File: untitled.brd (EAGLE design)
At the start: 42.2 x 27.9 mm, 15 parts, among them IC1 ACS758LCB-050B-PFF-T, IC2 LM2936DT-3.3

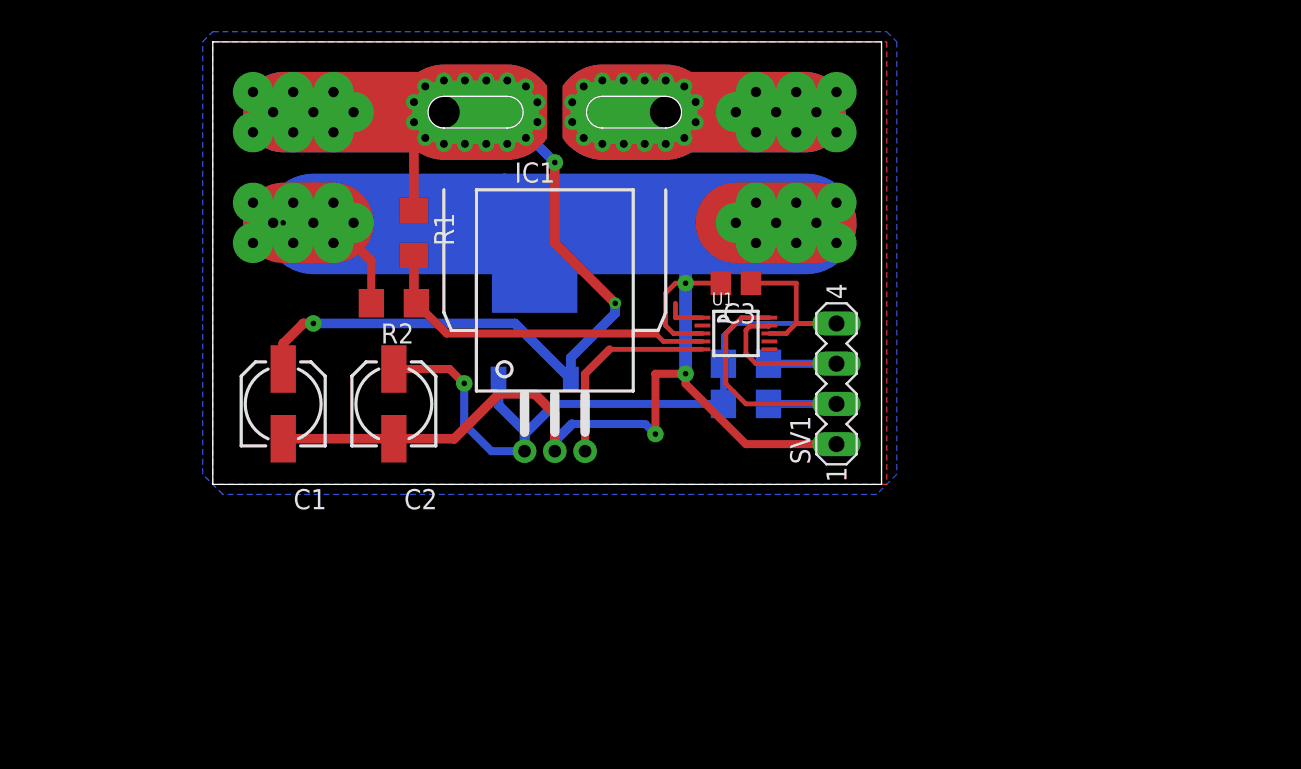
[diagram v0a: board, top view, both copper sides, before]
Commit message: Add new schematic for new dc dc converter
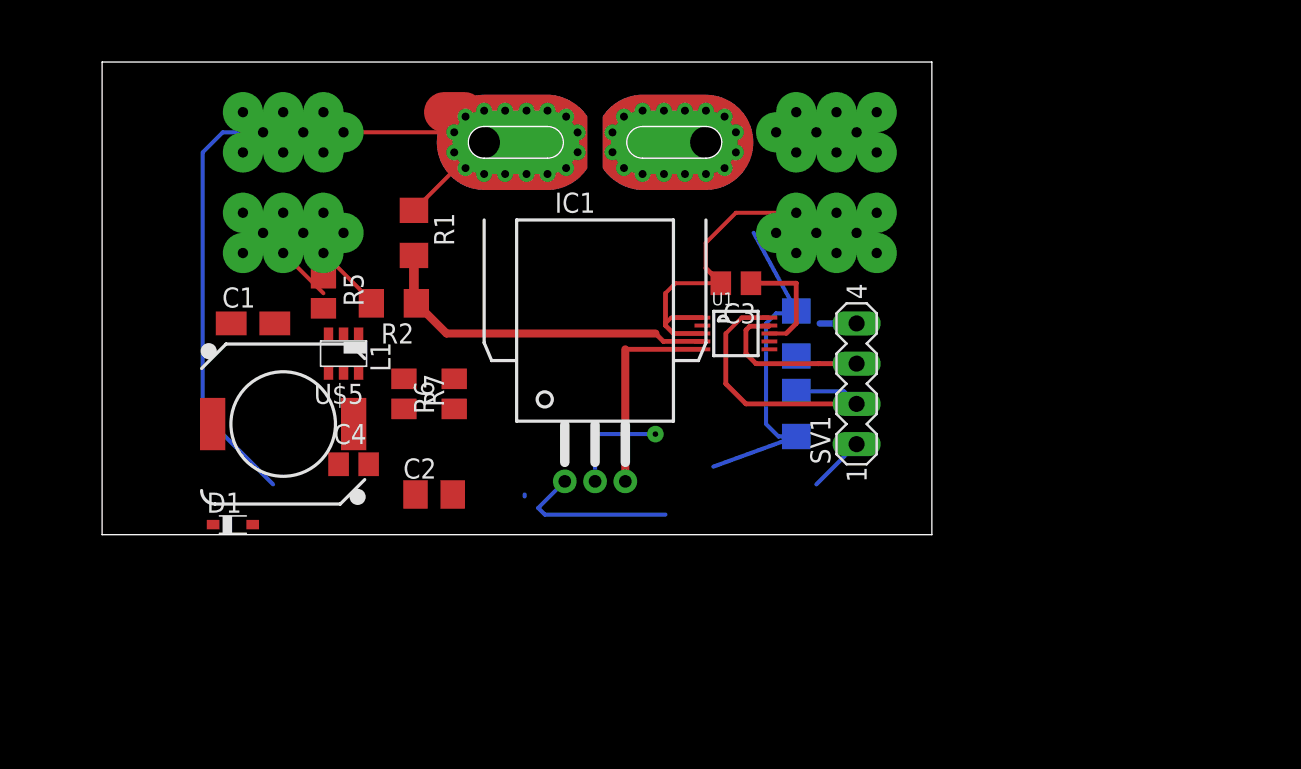
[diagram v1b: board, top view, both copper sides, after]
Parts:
- removed IC2: LM2936DT-3.3, national-semiconductor:TO252
- added C4: 100nF, rcl:C0805
- added D1: MBRS1100T3G, diode:SOD323_ST
- added L1: SRU1048-470Y, inductors:DR1030
- added R5: 100k, rcl:M0805
- added R6: 33k1, rcl:M0805
- added R7: 10k, rcl:M0805
- added U$5: LMR16006, texas:TSOT23-6_DDC
- C1: value (none) -> 2.2uF 12061C225K4T2A; device rcl:153CLV-0505 -> rcl:A/3216-18R
- C2: value (none) -> 22uF C2012X5R1C226M125AC; device rcl:153CLV-0505 -> rcl:R/2012-12R
- moved C2 6.25 mm to (15.2, 21.6), turned to 0 degrees
- moved C1 5.43 mm to (3.81, 32.4), turned to 0 degrees
- moved R4 3.70 mm to (38.1, 31.8), turned to 90 degrees
- moved R3 3.24 mm to (38.1, 26.7), turned to 270 degrees
- moved IC1 3.18 mm to (25.4, 43.8)
- moved U$1 2.84 mm to (34.3, 44.5)
- moved U$4 2.62 mm to (34.3, 38.1)
- moved U$3 1.42 mm to (12.1, 44.5)
- moved SV1 1.27 mm to (41.9, 28.6)
- moved U$2 0.90 mm to (12.1, 38.1)
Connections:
- new net N$10: C4.2, U$5.1
- new net N$11: R6.2, R7.1, U$5.3
- new net N$3: R5.1, U$5.4
- new net N$9: C4.1, D1.C, L1.2, U$5.6
- net GND: now also D1.A, R7.2, U$5.2; no longer IC2.2
- net N$4: now also R5.2, U$5.5; no longer IC2.1
- net VCC: now also L1.1, R6.1; no longer IC2.3
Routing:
- net GND: track 140.7 -> 44.0 mm, vias 4 -> 2
- net N$4: track 78.7 -> 45.3 mm, vias 3 -> 0
- net N$2: track 17.7 -> 0.08 mm
- net VCC: track 53.2 -> 42.4 mm, vias 1 -> 0
- net N$6: track 18.1 -> 19.3 mm
- net N$5: track 13.4 -> 14.3 mm
- removed copper zone on layer 1, net GND
- removed copper zone on layer 16, net GND
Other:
- board size 42.2 x 27.9 mm -> 52.4 x 29.8 mm

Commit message: Update board layout
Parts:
- moved R6 16.1 mm to (1.27, 33.0), turned to 0 degrees
- moved R7 13.9 mm to (1.27, 34.9), turned to 180 degrees
- moved C4 12.2 mm to (8.26, 35.6), turned to 180 degrees
- moved C1 8.89 mm to (12.7, 32.4), turned to 180 degrees
- moved R5 7.75 mm to (1.91, 29.8)
- moved D1 6.84 mm to (5.08, 26.0), turned to 270 degrees
- moved L1 6.35 mm to (12.1, 26.0)
- moved U$5 5.12 mm to (5.08, 33.0)
- moved C2 4.96 mm to (19.1, 24.8), turned to 90 degrees
- moved R2 4.26 mm to (14.6, 37.5), turned to 90 degrees
- moved R1 3.24 mm to (17.1, 37.5)
- moved U$2 2.69 mm to (10.2, 40.0)
- moved U$3 2.29 mm to (10.2, 45.7)
- moved IC1 0.64 mm to (25.4, 44.5)
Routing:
- net GND: track 44.0 -> 93.1 mm, vias 2 -> 1
- net VCC: track 42.4 -> 62.5 mm
- net N$9: track 0.00 -> 13.6 mm
- net N$2: track 0.08 -> 7.68 mm
- net N$4: track 45.3 -> 51.5 mm, vias 0 -> 3
- net N$11: track 0.00 -> 4.33 mm
- net N$3: track 0.00 -> 2.63 mm
- net N$10: track 0.00 -> 1.82 mm
- net N$1: track 13.2 -> 12.6 mm
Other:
- board size 52.4 x 29.8 mm -> 47.3 x 29.8 mm

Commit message: Update components
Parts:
- removed C2: 22uF C2012X5R1C226M125AC, rcl:R/2012-12R
- removed L1: SRU1048-470Y, inductors:DR1030
- added C5: 22uF 100V, rcl:150CLZ-0810
- added L2: 100uH, inductors:DR125
- C1: value 2.2uF 12061C225K4T2A -> 47uF 16v; device rcl:A/3216-18R -> rcl:153CLV-0505
- C3: value (none) -> 100nF
- R3, R4: value (none) -> 10k
- moved C1 13.5 mm to (0.00, 27.9), turned to 90 degrees
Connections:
- net GND: now also C5.-; no longer C2.-
- net N$4: now also C5.+; no longer C1.+
- net N$9: now also L2.1; no longer L1.2
- net VCC: now also C1.+, L2.2; no longer C2.+, L1.1
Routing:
- net N$7: track 0.00 -> 13.3 mm
- net N$4: track 51.5 -> 41.9 mm, vias 3 -> 2
- net N$12: track 0.00 -> 8.26 mm
- net N$8: track 0.00 -> 7.62 mm
- net VCC: track 62.5 -> 58.1 mm
- net GND: track 93.1 -> 89.1 mm
- net N$9: track 13.6 -> 11.8 mm
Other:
- board size 47.3 x 29.8 mm -> 56.2 x 29.8 mm

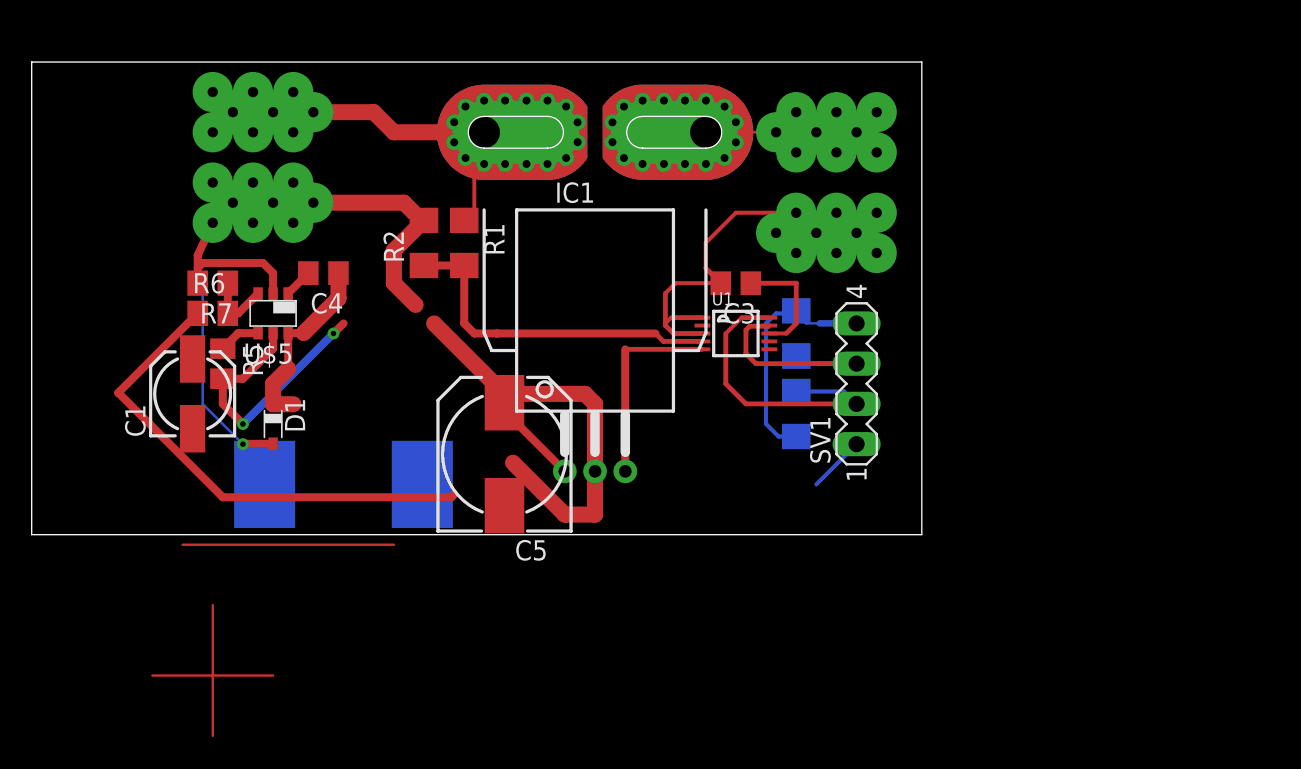
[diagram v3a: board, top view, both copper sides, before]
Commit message: Update capacitors
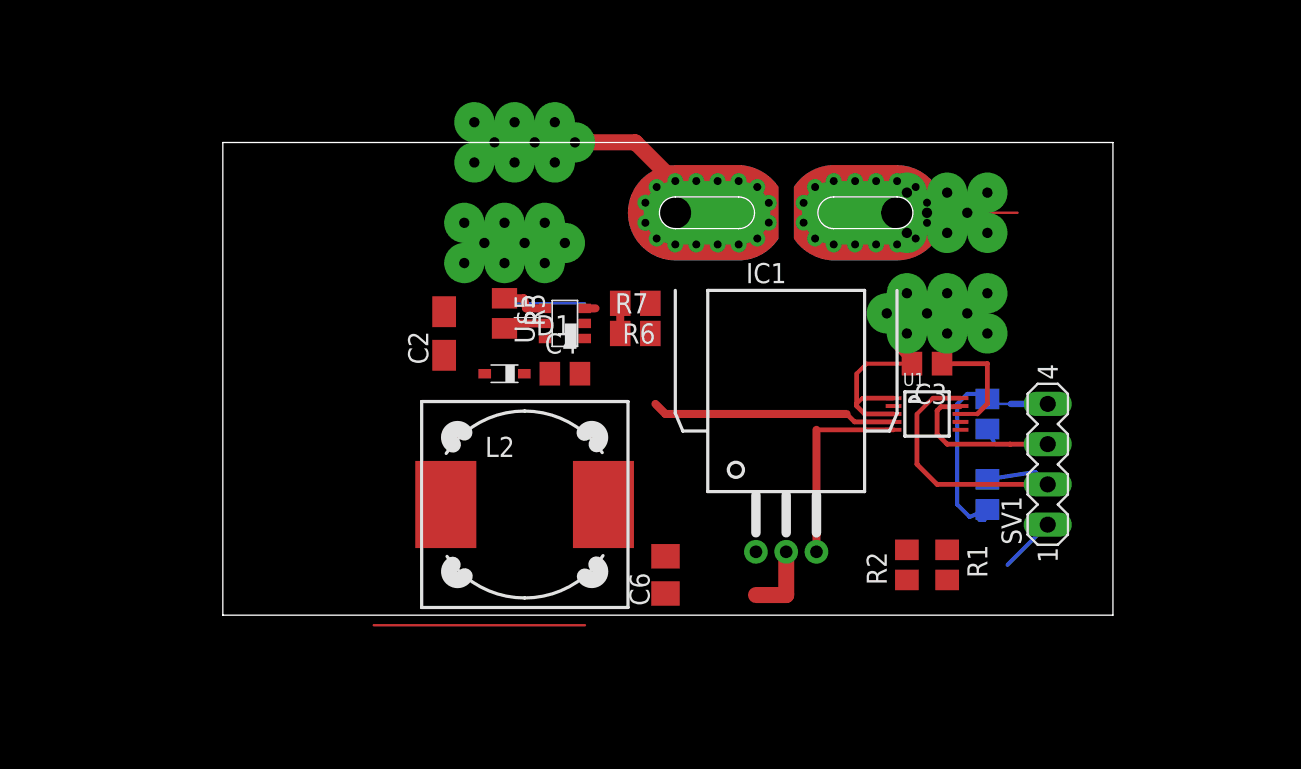
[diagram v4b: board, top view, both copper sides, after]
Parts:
- removed C1: 47uF 16v, rcl:153CLV-0505
- removed C5: 22uF 100V, rcl:150CLZ-0810
- added C2: 2.2uF 100V, rcl:A/3216-18R
- added C6: 22uF 25V, rcl:R/2012-12R
- R1, R2, R3, R4: device rcl:R1206 -> rcl:R0805
- moved R1 36.6 mm to (47.6, 17.1)
- moved R2 36.6 mm to (45.1, 17.1)
- moved R7 26.9 mm to (27.9, 31.8), turned to 0 degrees
- moved R6 26.7 mm to (27.9, 33.7), turned to 180 degrees
- moved U$5 18.4 mm to (23.5, 32.4), turned to 90 degrees
- moved R5 18.1 mm to (19.7, 33.0)
- moved C4 16.5 mm to (23.5, 29.2), turned to 0 degrees
- moved D1 14.9 mm to (19.7, 29.2), turned to 180 degrees
- moved IC1 13.1 mm to (37.5, 39.4)
- moved SV1 13.1 mm to (54.0, 23.5)
- moved R3 13.1 mm to (50.2, 21.6)
- moved U$1 13.1 mm to (46.4, 39.4)
- moved C3 13.1 mm to (46.4, 29.8)
- moved R4 13.1 mm to (50.2, 26.7)
- moved U$4 13.1 mm to (46.4, 33.0)
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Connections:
- net GND: now also C2.-, C6.-; no longer C1.-, C5.-
- net N$4: now also C2.+; no longer C5.+
- net VCC: now also C6.+; no longer C1.+
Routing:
- net GND: track 89.1 -> 37.3 mm, vias 1 -> 0
- net VCC: track 58.1 -> 23.8 mm
- net N$4: track 41.9 -> 19.3 mm, vias 2 -> 0
- net N$9: track 11.8 -> 0.00 mm
- net N$12: track 8.26 -> 0.00 mm
- net N$8: track 7.62 -> 0.00 mm
- net N$13: track 22.0 -> 15.5 mm
- net N$10: track 1.82 -> 0.00 mm
- net N$11: track 4.33 -> 2.59 mm

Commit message: Replace inductor with smaller one 10x10
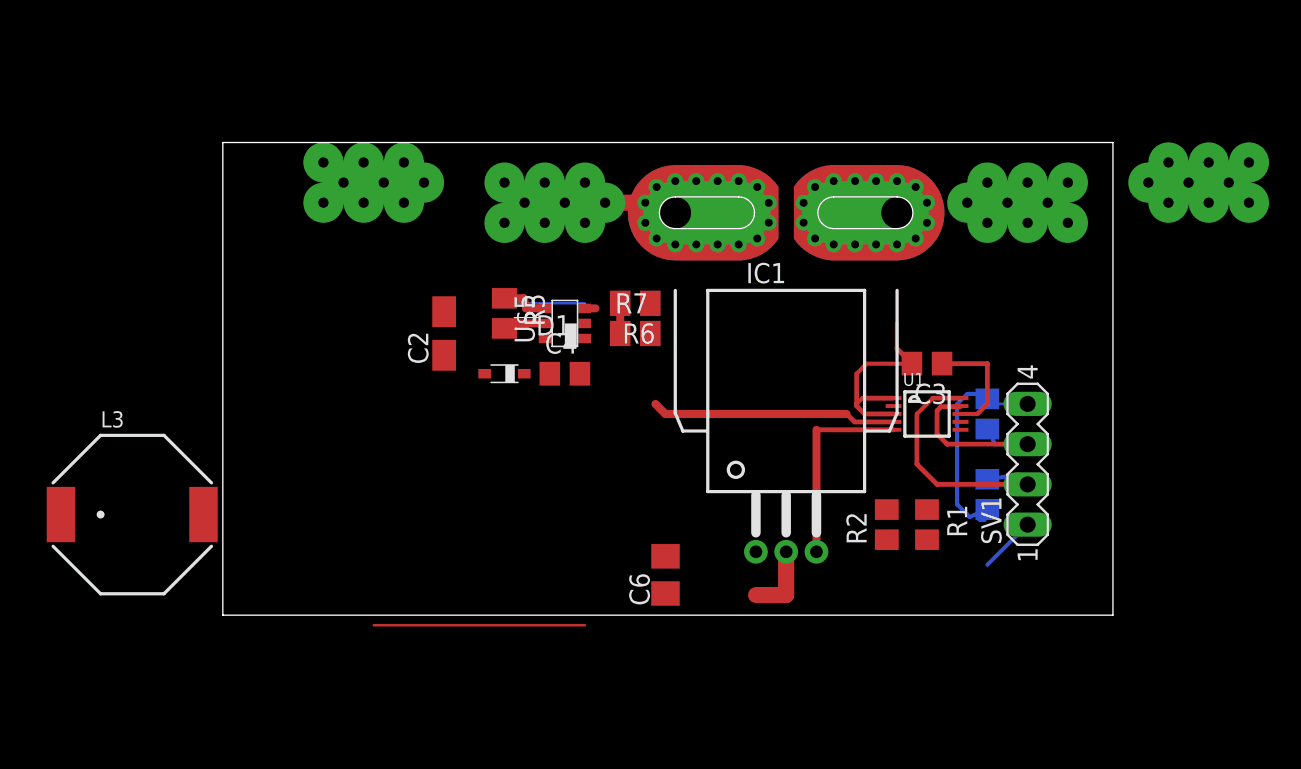
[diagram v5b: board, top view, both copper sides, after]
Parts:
- removed L2: 100uH, inductors:DR125
- added L3: SRU1038, inductor-bourns:SRU1038
- moved U$4 18.5 mm to (62.9, 41.3)
- moved U$2 9.67 mm to (12.1, 41.3)
- moved U$1 5.12 mm to (51.4, 40.0)
- moved U$3 4.26 mm to (23.5, 40.0)
- moved R1 2.84 mm to (46.4, 19.7)
- moved R2 2.84 mm to (43.8, 19.7)
- moved SV1 1.27 mm to (52.7, 23.5)
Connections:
- net N$9: now also L3.1; no longer L2.1
- net VCC: now also L3.2; no longer L2.2
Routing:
- net N$2: track 7.68 -> 0.08 mm
- net GND: track 37.3 -> 33.3 mm
- net N$4: track 19.3 -> 15.8 mm
- net N$6: track 19.3 -> 16.7 mm
- net N$5: track 14.7 -> 12.2 mm
- net VCC: track 23.8 -> 22.5 mm

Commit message: Add board layout
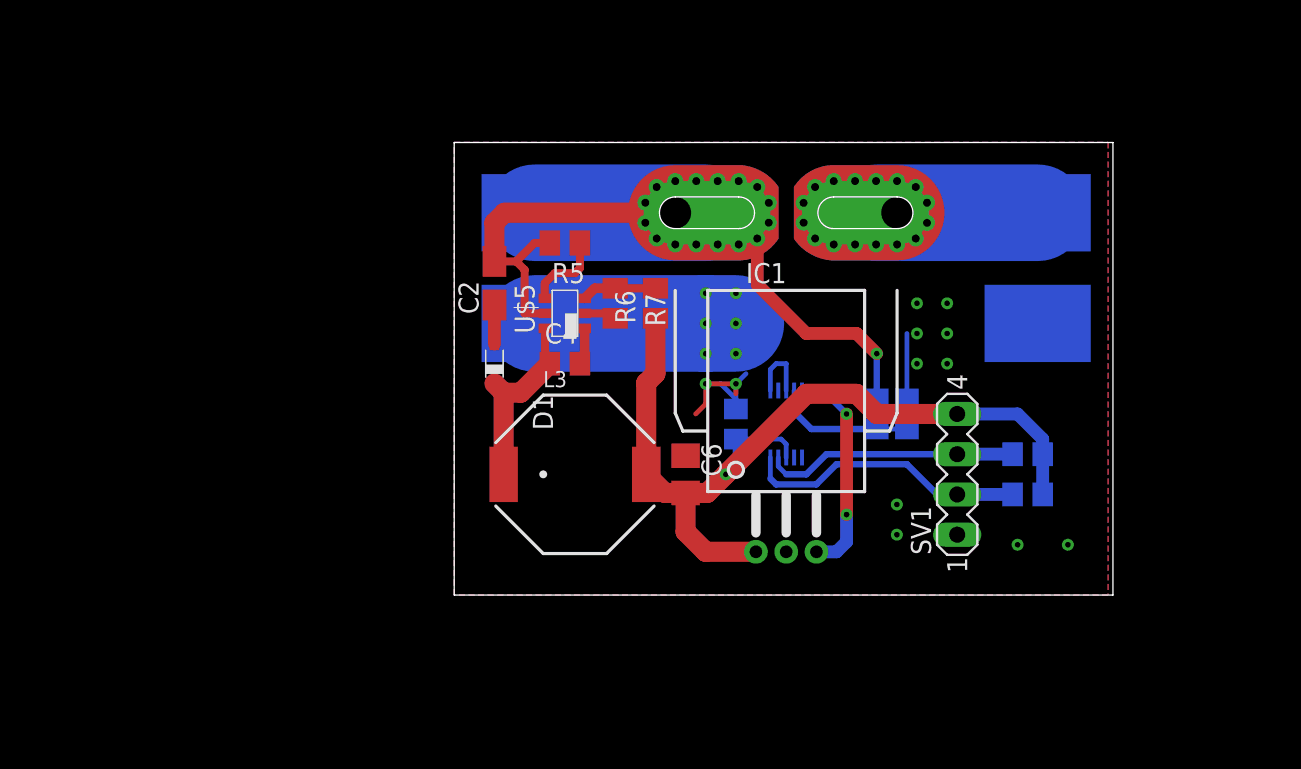
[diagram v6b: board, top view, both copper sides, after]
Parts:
- removed U$1, U$3: PADPAD, wirepad:PADHOLES
- added IN, OUT: PADSMD, wirepad:PADS
- U$2, U$4: value PADPAD -> PADSMD; device wirepad:PADHOLES -> wirepad:PADS
- moved L3 28.1 mm to (24.1, 22.9)
- moved U$2 13.0 mm to (21.6, 32.4), flipped to the bottom
- moved U$4 13.0 mm to (53.3, 32.4), flipped to the bottom
- moved C3 12.7 mm to (34.3, 26.0), flipped to the bottom, turned to 90 degrees
- moved U1 8.91 mm to (37.5, 26.0), flipped to the bottom, turned to 180 degrees
- moved R1 7.67 mm to (43.2, 26.7), flipped to the bottom
- moved R2 7.10 mm to (45.1, 26.7), flipped to the bottom
- moved C6 6.48 mm to (31.1, 22.9), turned to 270 degrees
- moved R5 5.85 mm to (23.5, 37.5), turned to 180 degrees
- moved SV1 4.49 mm to (48.3, 22.9)
- moved C2 4.49 mm to (19.1, 34.9)
- moved R4 3.59 mm to (52.7, 24.1), turned to 180 degrees
- moved R3 2.54 mm to (52.7, 21.6), turned to 180 degrees
- moved R7 2.29 mm to (26.7, 33.7), turned to 270 degrees
- moved R6 1.27 mm to (29.2, 33.7), turned to 90 degrees
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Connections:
- net GND: now also U$2.P$1, U$4.P$1; no longer U$2.P$10, U$2.P$11, U$2.P$12, U$2.P$2, U$2.P$3, U$2.P$5, U$2.P$6, U$2.P$7, U$2.P$9, U$4.P$10, U$4.P$11, U$4.P$12, U$4.P$2, U$4.P$3, U$4.P$5, U$4.P$6, U$4.P$7, U$4.P$9
- net N$2: now also OUT.P$1; no longer U$1.P$10, U$1.P$11, U$1.P$12, U$1.P$2, U$1.P$3, U$1.P$5, U$1.P$6, U$1.P$7, U$1.P$9
- net N$4: now also IN.P$1; no longer U$3.P$10, U$3.P$11, U$3.P$12, U$3.P$2, U$3.P$3, U$3.P$5, U$3.P$6, U$3.P$7, U$3.P$9
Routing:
- net N$4: track 15.8 -> 56.7 mm, vias 0 -> 1
- net VCC: track 22.5 -> 57.2 mm, vias 0 -> 1
- net N$7: track 13.3 -> 0.00 mm
- net N$9: track 0.00 -> 12.0 mm
- net N$2: track 0.08 -> 10.2 mm
- net N$13: track 15.5 -> 8.91 mm
- net N$5: track 12.2 -> 16.1 mm
- net N$10: track 0.00 -> 2.35 mm
- net GND: track 33.3 -> 35.7 mm, vias 0 -> 18
- net N$11: track 2.59 -> 4.73 mm
- net N$3: track 3.07 -> 5.19 mm
- net N$6: track 16.7 -> 18.1 mm
- net N$1: track 12.6 -> 13.7 mm, vias 0 -> 2
- added copper zone on layer 1, net GND
- added copper zone on layer 16, net GND
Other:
- board size 56.2 x 29.8 mm -> 41.6 x 28.6 mm
